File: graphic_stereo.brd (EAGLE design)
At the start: 109 x 29.5 mm, 73 parts, among them IC1 NE5532D, IC2 NE5532D, IC3 NE5532D, IC4 NE5532D, IC5 NE5532D

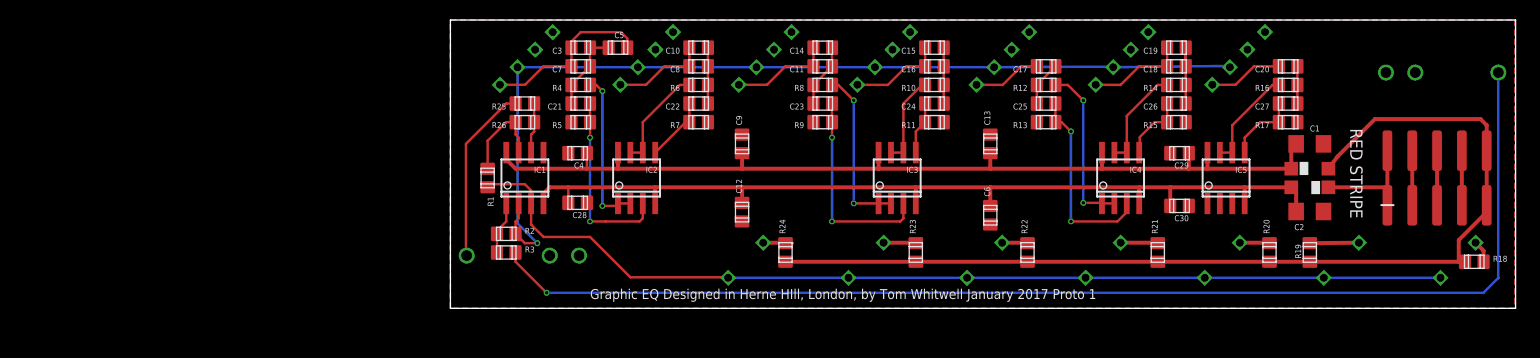
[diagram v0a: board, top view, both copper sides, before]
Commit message: Creating experimental stereo output versions
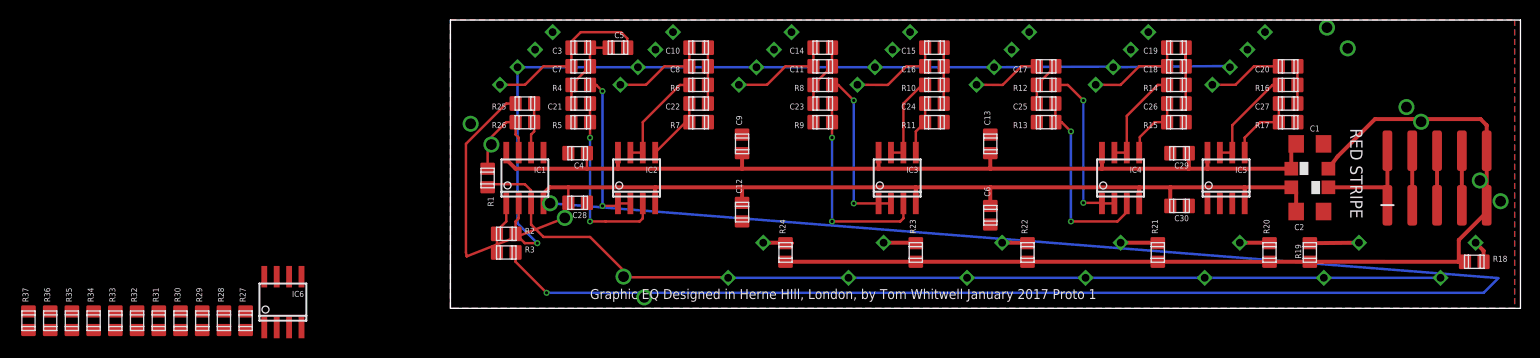
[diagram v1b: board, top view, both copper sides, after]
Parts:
- added IC6: NE5532D, linear:SO08
- added L_OUT, R_OUT: THONKICONNNEW, MusicThingModular:WQP-PJ301M-12_JACK
- added R27, R28: 470R, we-rcl:C0805
- added R29, R30, R31, R32, R33, R34, R35, R36, R37: 2.7k, we-rcl:C0805
- moved OUTPUT 96.1 mm to (6.67, 14.3), turned to 135 degrees
- moved INPUT 8.58 mm to (15.2, 5.71), turned to 315 degrees
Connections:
- new net N$1: IC6.1, R27.2, R29.1
- new net N$22: L_OUT.P$1_TIP, R27.1
- new net N$44: R28.1, R_OUT.P$1_TIP
- new net N$46: IC6.7, R28.2, R30.1
- new net N$47: IC6.6, R30.2, R32.2, R34.2, R36.2
- new net N$49: IC6.2, R29.2, R31.2, R33.2, R35.2, R37.2
- net +12V: now also IC6.8
- net -12V: now also IC6.4
- net GND: now also IC6.3, IC6.5, L_OUT.P$3_SLEEVE, R_OUT.P$3_SLEEVE
- net N$21: now also R33.1
- net N$26: now also R31.1
- net N$27: now also R34.1
- net N$29: now also R32.1
- net N$33: now also R35.1
- net N$35: now also R36.1
- net N$39: now also R37.1
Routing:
- net N$6: track 124.5 -> 200.8 mm
- net N$2: track 18.4 -> 29.1 mm
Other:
- board size 109 x 29.5 mm -> 109.5 x 29.5 mm
